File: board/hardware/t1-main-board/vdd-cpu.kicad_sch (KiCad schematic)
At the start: 20 parts, among them U1201 TPS6286910CRQYR

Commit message: vdd_cpu on the TPS62870Z4 (ADR 0026, placement v1.5)
ADR 0026 supersedes ADR 0023: TPS62870Z4WRXSR at I2C0 0x42 with the
Coilcraft XEL4012-920NE, 3 MHz, MODE/SYNC to ground with forced PWM by
register, differential sense from the 22 uF at the SoC. Output capacitance
sized at the 1.1 V devicetree cap for the 4.8 A worst-case step (peak
1.149 V, DC-bias effective values); 1800 MHz kept as a verification row.

Submodule at libs v0.3.2 (the RXS0016A land). BOM v1.18 item 8, power
tree v0.10, pinout v1 I2C0 note, feature blocks #13, placement v1.5.
Schematic regenerated, board rebuilt: 991 parts placed, 97.0 % board need,
factor 1.71, 244 capacitors within their bound, DRC 0 errors, ERC 0
errors, craft Q1 met, pcb tests pass, STEP exported (27 parts without a
model in KiCad's library, as before).

Co-Authored-By: Claude Opus 5.5 <noreply@anthropic.com>
Claude-Session: https://claude.ai/code/session_013P6pW9LdyEMFishwCcZGUr
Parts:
- removed R1205: 100 kΩ, Resistor_SMD:R_0201_0603Metric, symbol Device:R
- removed R1206: 86.6 kΩ, Resistor_SMD:R_0201_0603Metric, symbol Device:R
- added C1208: 22 µF, Capacitor_SMD:C_0603_1608Metric, symbol Device:C
- added NT1202: NetTie, NetTie:NetTie-2_SMD_Pad0.5mm, symbol Device:NetTie_2
- C1201: value 100 nF -> 47 µF; footprint Capacitor_SMD:C_0402_1005Metric -> Capacitor_SMD:C_0603_1608Metric; MPN GRM155R71C104KA88D -> GRM188R60J476ME15D; Spec (none) -> 6.3 V X5R
- C1202: value 10 µF -> 100 nF; footprint Capacitor_SMD:C_0603_1608Metric -> Capacitor_SMD:C_0201_0603Metric; MPN C1608X7R1A106K080AC -> GRM033R61A104KE15D; Manufacturer TDK -> Murata; Spec 10 V X7R -> 10 V X5R
- C1203: value 10 µF -> 47 µF; MPN C1608X7R1A106K080AC -> GRM188R60J476ME15D; Manufacturer TDK -> Murata; Spec 10 V X7R -> 6.3 V X5R
- C1204: Spec (none) -> 10 V X5R
- C1205: value 22 µF -> 100 nF; footprint Capacitor_SMD:C_0603_1608Metric -> Capacitor_SMD:C_0201_0603Metric; MPN GRM188R60J226MEA0D -> GRM033R61A104KE15D; Spec 6.3 V X5R -> 10 V X5R
- C1206: value 22 µF -> 5.6 nF; footprint Capacitor_SMD:C_0603_1608Metric -> Capacitor_SMD:C_0402_1005Metric; MPN GRM188R60J226MEA0D -> GRM1555C1H562JE01D; Spec 6.3 V X5R -> 50 V C0G
- C1207: value 100 nF -> 22 pF; footprint Capacitor_SMD:C_0201_0603Metric -> Capacitor_SMD:C_0402_1005Metric; MPN GRM033R61A104KE15D -> GRM1555C1H220JA01D; Spec (none) -> 50 V C0G
- L1201: value 220 nH -> 92 nH; MPN XGL4012-221MEC -> XEL4012-920NEC; Spec Isat 9.9 A -> Isat 24 A
- R1202: value 100 Ω -> 82.5 Ω; MPN RC0201FR-07100RL -> RC0201FR-0782R5L
- R1203: value 0 Ω -> 5 mΩ; footprint Resistor_SMD:R_0402_1005Metric -> Resistor_SMD:R_1206_3216Metric; Alternate vos-local-sense -> (none); Constraints (none) -> PCB-T-02; MPN RC0402JR-070RL -> WSL12065L000FEA; Manufacturer YAGEO -> Vishay Dale; Spec (none) -> 1206; now fitted
- R1204: value 5 mΩ -> 100 kΩ; footprint Resistor_SMD:R_1206_3216Metric -> Resistor_SMD:R_0201_0603Metric; Constraints PCB-T-02 -> (none); MPN WSL12065L000FEA -> RC0201FR-07100KL; Manufacturer Vishay Dale -> YAGEO; Spec 1206 -> (none)
- TP1201: value VDD_CPU_VOS -> VDD_CPU_SRC; footprint T1_Main_Board:TestPoint_Pad_D0.8mm -> TestPoint:TestPoint_Pad_D1.0mm
- TP1202: value VDD_CPU_SRC -> vdd_cpu
- TP1203: value vdd_cpu -> VDD_CPU_PG; footprint TestPoint:TestPoint_Pad_D1.0mm -> T1_Main_Board:TestPoint_Pad_D0.8mm
- TP1204: value VDD_CPU_PG -> VDD_CPU_VOS
- U1201: value TPS6286910CRQYR -> TPS62870Z4WRXSR; footprint texas-instruments:Texas_RQY0009A_VQFN-HR-9_1.5x2.5mm_P0.5mm -> texas-instruments:Texas_RXS0016A_VQFN-FCRLF-16_2.55x3.55mm_P0.5mm; symbol texas-instruments:TPS6286910CRQYR -> texas-instruments:TPS62870Z4WRXSR; MPN TPS6286910CRQYR -> TPS62870Z4WRXSR; MPN_2 TPS628691ARQYR -> (none); Manufacturer_2 Texas Instruments -> (none); Second_Source Texas Instruments TPS628691ARQYR (same land; pin 9 is VSET/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 -> (none)
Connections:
- net GND: now also U1201.11 (MODE/SYNC), U1201.17 (GND), U1201.6 (GND), U1201.8 (GND), C1208.2, NT1202.2; no longer C1206.2, C1207.2, U1201.1 (AGND), U1201.2 (PGND)
- net I2C0_SCL: now also U1201.13 (SCL); no longer U1201.6 (SCL)
- net I2C0_SDA: now also U1201.12 (SDA); no longer U1201.5 (SDA)
- net VDD_CPU_PG: now also R1204.2, TP1203.1, U1201.10 (PG); no longer TP1204.1, U1201.9 (PG)
- net VSYS_LV: now also C1204.1, U1201.15 (VSEL), U1201.16 (FSEL), U1201.5 (VIN), U1201.9 (VIN); no longer U1201.3 (VIN)
- net vcca1v8_pmu: now also R1204.1
- net vdd_cpu: now also R1203.2, TP1202.1; no longer R1204.2, TP1203.1
- net VDD_CPU_EN: now reaches R1201.2, U1201.4 (EN)
- net VDD_CPU_EN: now also C1205.1; no longer C1204.1
- new net VDD_CPU_CC: C1206.1, R1202.2
- new net VDD_CPU_COMP: C1207.1, R1202.1, U1201.1 (COMP)
- new net VDD_CPU_GOS: C1206.2, C1207.2, NT1202.1, U1201.2 (GOSNS)
- new net VDD_CPU_SRC: C1208.1, L1201.2, R1203.1, TP1201.1
- new net VDD_CPU_VOS: NT1201.1, TP1204.1, U1201.3 (VOSNS)
- no-connect marks 0 -> 1
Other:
- note added: "Enable and compensation (items 1, 4)"
- note added: "Output (items 2, 4)"
- note added: "Power good pull-up (item 1)"
- note added: "Remote sense at the SoC capacitor (item 5)"
- note added: "TPS62870Z4 at I2C0 0x42 (ADR 0026 item 1)"
- note added: "Test pads"
- note removed: "Enable, control"
- note removed: "Input"
- note removed: "Output and sense"
- note removed: "Power good (item 6)"
- moved on the sheet: C1201, C1202, C1203, C1204, C1205, C1206, C1207, L1201, NT1201, R1201, R1202, R1204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

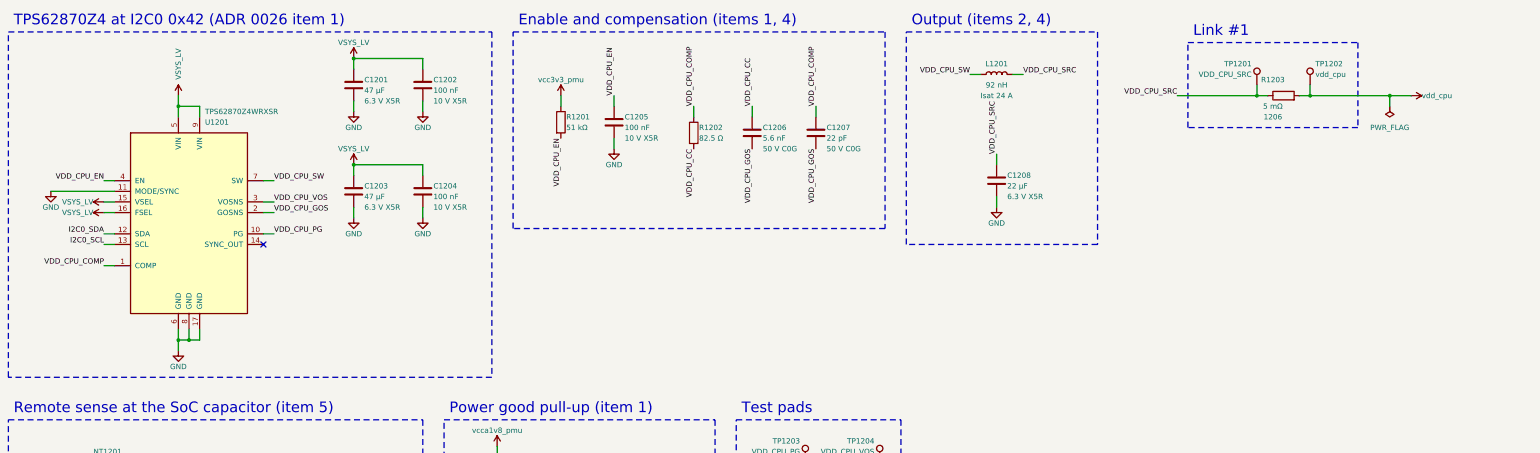
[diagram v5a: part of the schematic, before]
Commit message: Schematic: side-pin grounds drop below their pin; shield frames in one group
A ground on an IC's side pin whose next row is taken (U1201 MODE/SYNC on
blk.vdd-cpu, U2801 VNEG/FBN on blk.hpa-rails-pre) leaves on a stub past
its neighbours' text and drops to the first free row, its GND symbol
pointing down below the pin instead of hanging among the neighbours'
labels (CRAFT-85); a ground below it on the same side joins the drop.
The shield-can frames share one group sized from its contents
(CRAFT-174) instead of three groups as wide as their titles. Other
sheets change only in #PWR numbering.

Generated twice, identical. ERC 0 errors (9 warnings, as before), craft
Q1 met (Q2 reached), overlaps 0 collisions; both sheets checked on
200 dpi PDF crops. References unchanged, so the board is not rebuilt.

Co-Authored-By: Claude Opus 5.5 <noreply@anthropic.com>
Claude-Session: https://claude.ai/code/session_013P6pW9LdyEMFishwCcZGUr
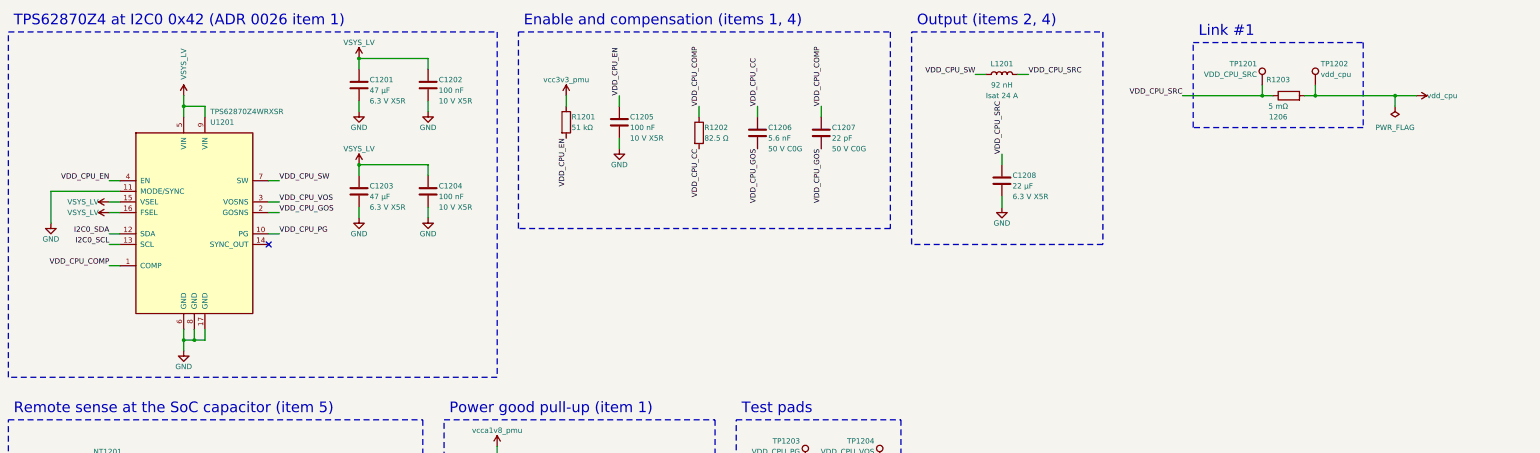
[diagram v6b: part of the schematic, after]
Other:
- moved on the sheet: C1201, C1202, C1203, C1204, C1205, C1206, C1207, C1208, L1201, R1201, R1202, R1203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

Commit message: Board: pre-PCB schematic items closed with datasheets (BOM v1.22)
Display INA236 to 0x49 (INA236B, A0 = VS): no A0 = SDA strap, so the
address no longer depends on the host's I2C hold time. The 18 WSL
shunts and links on Vishay's doc 30100 lands. 24 MHz crystal NDK
NX3225GA (CL 8 pF) with 2 x 10 pF. Backlight inductor Coilcraft
XFL3012-223MEC on its published land (no placeholder left). Action
button PTS815 G code on the side-button land. Cover-detect leakage,
TPS3808 spread, RP2354A supply pins and the USB series scheme closed
without change. Placement v1.9: 100.2 % need, factor 1.64, DRC 0
errors; power tree v0.12; PCB-Z-08 and CB-08 strip values.

Co-Authored-By: Claude Opus 5.5 <noreply@anthropic.com>
Claude-Session: https://claude.ai/code/session_013P6pW9LdyEMFishwCcZGUr
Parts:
- R1203: footprint Resistor_SMD:R_1206_3216Metric -> T1_Main_Board:R_Vishay_WSL1206_2m-5m9
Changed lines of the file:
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@@
   (property "Value" "5 mΩ" (at 326.39 53.34 90) (effects (font (size 1.27 1.27))))
   (property "Spec" "1206" (at 326.39 55.88 90) (effects (font (size 1.27 1.27))))
-  (property "Footprint" "Resistor_SMD:R_1206_3216Metric" (at 328.93 50.8 0) (effects (font (size 1.27 1.27))) (hide yes))
+  (property "Footprint" "T1_Main_Board:R_Vishay_WSL1206_2m-5m9" (at 328.93 50.8 0) (effects (font (size 1.27 1.27))) (hide yes))
   (property "Datasheet" "https://www.vishay.com/docs/30100/wsl.pdf" (at 328.93 50.8 0) (effects (font (size 1.27 1.27))) (hide yes))
   (property "Description" "Current-sense resistor, 5 mOhm, 1 %, 0.5 W, 1206 metal strip: measurement link H5" (at 328.93 50.8 0) (effects (font (size 1.27 1.27))) (hide yes))
